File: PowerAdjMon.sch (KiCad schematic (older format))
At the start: 11 parts

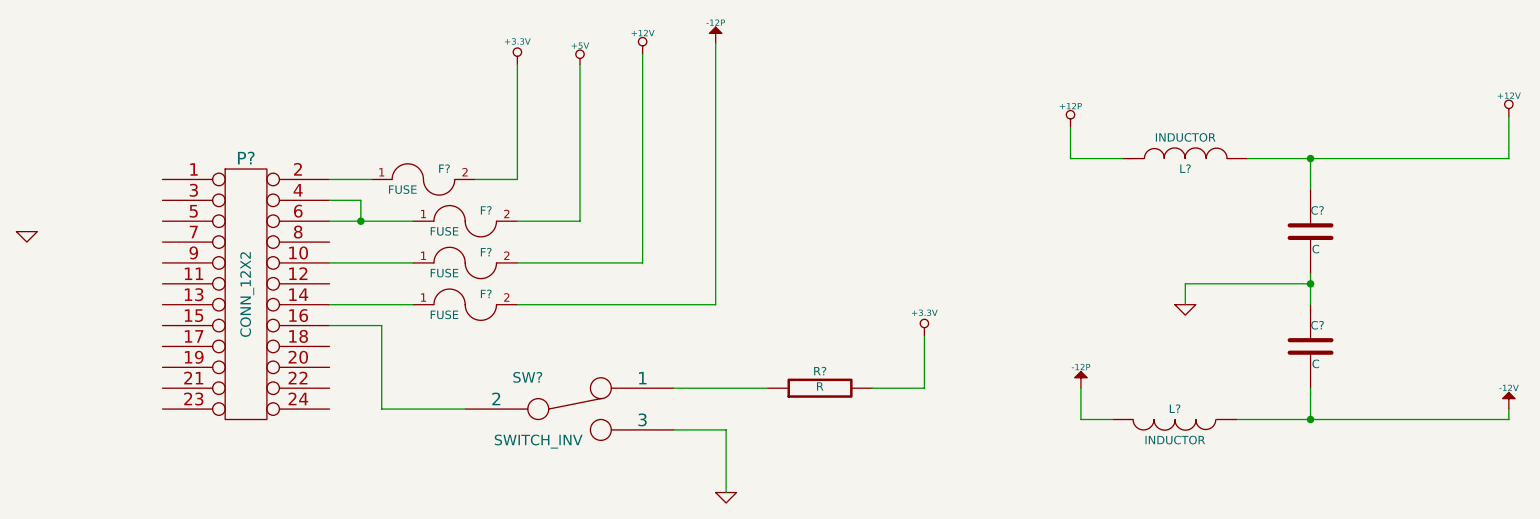
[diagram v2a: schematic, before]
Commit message: Fan/Current mode redo
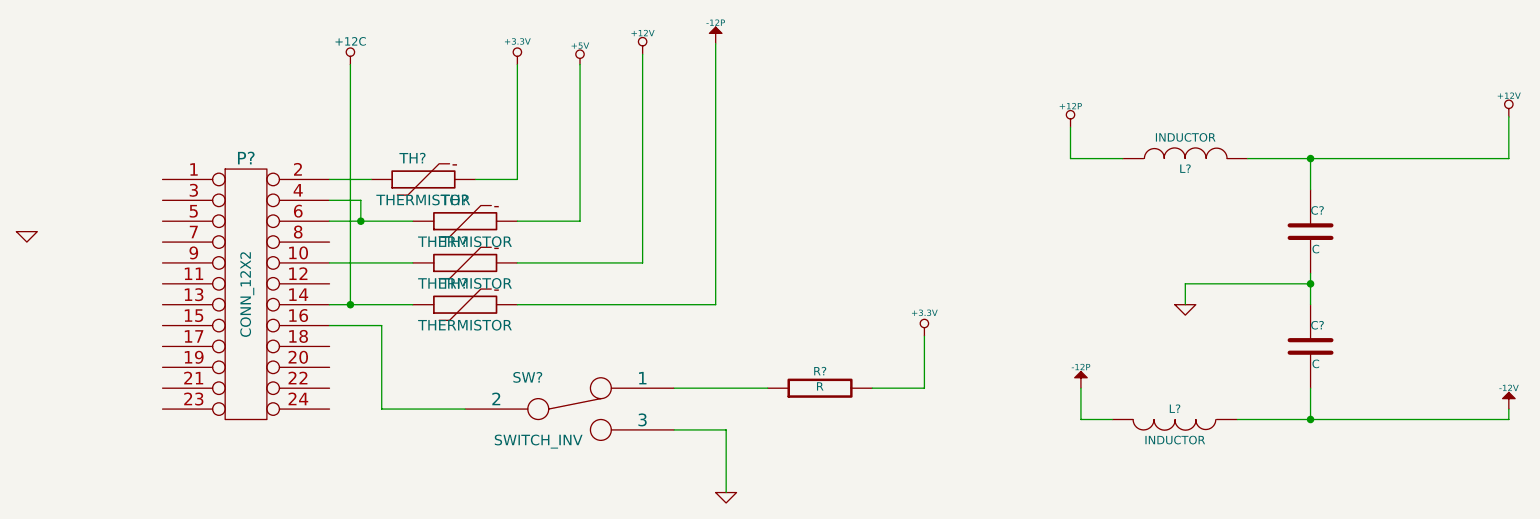
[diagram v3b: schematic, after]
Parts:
- removed F? (x4): FUSE, ~, symbol FUSE
- added TH? (x4): THERMISTOR, symbol THERMISTOR
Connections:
- net +12V: now also TH?.2
- net +3.3V: now also TH?.2
- net +5V: now also TH?.2
- net -12P: now also TH?.2
- net at P?.10 (P10): now also TH?.1
- net +12C: now reaches P?.14 (P14)
- net +12C: now also TH?.1
- net at P?.2 (P2): now also TH?.1
- net at P?.4 (P4), P?.6 (P6): now also TH?.1
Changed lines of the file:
@@
-EESchema Schematic File Version 2  date Sat 08 Feb 2014 11:37:49 PM EST
+EESchema Schematic File Version 2  date Sun 09 Feb 2014 12:22:09 AM EST
 LIBS:power
 LIBS:device
@@
 $EndDescr
 $Comp
+L THERMISTOR TH?
+U 1 1 52F70C96
+P 3150 2250
+F 0 "TH?" V 3250 2300 50  0000 C CNN
+F 1 "THERMISTOR" V 3050 2250 50  0000 C CNN
+	1    3150 2250
+	0    -1   -1   0
+$EndComp
+$Comp
+L THERMISTOR TH?
+U 1 1 52F70C94
+P 3150 2050
+F 0 "TH?" V 3250 2100 50  0000 C CNN
+F 1 "THERMISTOR" V 3050 2050 50  0000 C CNN
+	1    3150 2050
+	0    -1   -1   0
+$EndComp
+$Comp
+L THERMISTOR TH?
+U 1 1 52F70C92
+P 3150 1850
+F 0 "TH?" V 3250 1900 50  0000 C CNN
+F 1 "THERMISTOR" V 3050 1850 50  0000 C CNN
+	1    3150 1850
+	0    -1   -1   0
+$EndComp
+$Comp
+L THERMISTOR TH?
+U 1 1 52F70C8B
+P 2950 1650
+F 0 "TH?" V 3050 1700 50  0000 C CNN
+F 1 "THERMISTOR" V 2850 1650 50  0000 C CNN
+	1    2950 1650
+	0    -1   -1   0
+$EndComp
+$Comp
+L +12C #PWR?
+U 1 1 52F70C06
+P 2600 1100
+F 0 "#PWR?" H 2600 1070 30  0001 C CNN
+F 1 "+12C" H 2600 1210 40  0000 C CNN
+	1    2600 1100
+	1    0    0    -1
+$EndComp
+Connection ~ 2600 2250
+Wire Wire Line
+	2600 2250 2600 1100
+Connection ~ 7200 2800
+Wire Wire Line
+	8150 2750 8150 2800
+Connection ~ 7200 1550
+Wire Wire Line
+	8150 1350 8150 1550
+Wire Wire Line
+	8150 1550 6900 1550
+Wire Wire Line
+	7200 1700 7200 1550
+Wire Wire Line
+	7200 2800 7200 2650
+Wire Wire Line
+	8150 2800 6850 2800
+Connection ~ 7200 2150
+Wire Wire Line
+	7200 2150 6600 2150
+Wire Wire Line
+	6600 2150 6600 2250
+Wire Wire Line
+	7200 2100 7200 2250
+Wire Wire Line
+	6300 1550 6050 1550
+Wire Wire Line
+	6050 1550 6050 1400
+Wire Wire Line
+	6250 2800 6100 2800
+Wire Wire Line
+	6100 2800 6100 2650
+Wire Wire Line
+	5350 2400 5350 2650
+Wire Wire Line
+	5350 2650 5100 2650
+Wire Wire Line
+	4150 2650 4600 2650
+Wire Wire Line
+	4400 3150 4400 2850
+Wire Wire Line
+	4400 2850 4150 2850
+Wire Wire Line
+	3150 2750 2750 2750
+Wire Wire Line
+	2750 2750 2750 2350
+Wire Wire Line
+	2750 2350 2500 2350
+Wire Wire Line
+	4350 1000 4350 2250
+Wire Wire Line
+	4350 2250 3400 2250
+Wire Wire Line
+	4000 1050 4000 2050
+Wire Wire Line
+	4000 2050 3400 2050
+Wire Wire Line
+	2500 2250 2900 2250
+Wire Wire Line
+	2500 2050 2900 2050
+Wire Wire Line
+	3700 1100 3700 1850
+Wire Wire Line
+	3700 1850 3400 1850
+Connection ~ 2650 1850
+Wire Wire Line
+	2650 1850 2650 1750
+Wire Wire Line
+	2650 1750 2500 1750
+Wire Wire Line
+	2500 1850 2900 1850
+Wire Wire Line
+	3400 1100 3400 1650
+Wire Wire Line
+	3400 1650 3200 1650
+Wire Wire Line
+	2500 1650 2700 1650
+$Comp
 L CONN_12X2 P?
 U 1 1 52F45305
@@
 F 1 "+5V" H 3700 1190 30  0000 C CNN
 	1    3700 1100
-	1    0    0    -1
-$EndComp
-$Comp
-L FUSE F?
-U 1 1 52F4550E
-P 2950 1650
-F 0 "F?" H 3050 1700 40  0000 C CNN
-F 1 "FUSE" H 2850 1600 40  0000 C CNN
-F 2 "~" H 2950 1650 60  0000 C CNN
-F 3 "~" H 2950 1650 60  0000 C CNN
-	1    2950 1650
-	1    0    0    -1
-$EndComp
-$Comp
-L FUSE F?
-U 1 1 52F4551B
-P 3150 1850
-F 0 "F?" H 3250 1900 40  0000 C CNN
-F 1 "FUSE" H 3050 1800 40  0000 C CNN
-F 2 "~" H 3150 1850 60  0000 C CNN
-F 3 "~" H 3150 1850 60  0000 C CNN
-	1    3150 1850
-	1    0    0    -1
-$EndComp
-$Comp
-L FUSE F?
-U 1 1 52F45521
-P 3150 2050
-F 0 "F?" H 3250 2100 40  0000 C CNN
-F 1 "FUSE" H 3050 2000 40  0000 C CNN
-F 2 "~" H 3150 2050 60  0000 C CNN
-F 3 "~" H 3150 2050 60  0000 C CNN
-	1    3150 2050
-	1    0    0    -1
-$EndComp
-$Comp
-L FUSE F?
-U 1 1 52F45527
-P 3150 2250
-F 0 "F?" H 3250 2300 40  0000 C CNN
-F 1 "FUSE" H 3050 2200 40  0000 C CNN
-F 2 "~" H 3150 2250 60  0000 C CNN
-F 3 "~" H 3150 2250 60  0000 C CNN
-	1    3150 2250
 	1    0    0    -1
 $EndComp
@@
 	1    0    0    -1
 $EndComp
-Wire Wire Line
-	2500 1650 2700 1650
-Wire Wire Line
-	3200 1650 3400 1650
-Wire Wire Line
-	3400 1650 3400 1100
-Wire Wire Line
-	2500 1850 2900 1850
-Wire Wire Line
-	2500 1750 2650 1750
-Wire Wire Line
-	2650 1750 2650 1850
-Connection ~ 2650 1850
-Wire Wire Line
-	3400 1850 3700 1850
-Wire Wire Line
-	3700 1850 3700 1100
-Wire Wire Line
-	2500 2050 2900 2050
-Wire Wire Line
-	2500 2250 2900 2250
 $Comp
 L +12V #PWR?
@@
 	1    0    0    -1
 $EndComp
-Wire Wire Line
-	3400 2050 4000 2050
-Wire Wire Line
-	4000 2050 4000 1050
 $Comp
 L -12P #PWR?
@@
 	1    0    0    -1
 $EndComp
-Wire Wire Line
-	3400 2250 4350 2250
-Wire Wire Line
-	4350 2250 4350 1000
 $Comp
 L R R?
@@
 	0    -1   -1   0
 $EndComp
-Wire Wire Line
-	2500 2350 2750 2350
-Wire Wire Line
-	2750 2350 2750 2750
-Wire Wire Line
-	2750 2750 3150 2750
 $Comp
 L GND #PWR?
@@
 	1    0    0    -1
 $EndComp
-Wire Wire Line
-	4150 2850 4400 2850
-Wire Wire Line
-	4400 2850 4400 3150
-Wire Wire Line
-	4150 2650 4600 2650
 $Comp
 L +3.3V #PWR?
@@
 	1    0    0    -1
 $EndComp
-Wire Wire Line
-	5100 2650 5350 2650
-Wire Wire Line
-	5350 2650 5350 2400
 $Comp
 L INDUCTOR L?
@@
 	1    0    0    -1
 $EndComp
-Wire Wire Line
-	6100 2650 6100 2800
-Wire Wire Line
-	6100 2800 6250 2800
-Wire Wire Line
-	6050 1400 6050 1550
-Wire Wire Line
-	6050 1550 6300 1550
-Wire Wire Line
-	7200 2100 7200 2250
-Wire Wire Line
-	6600 2150 6600 2250
-Wire Wire Line
-	6600 2150 7200 2150
-Connection ~ 7200 2150
-Wire Wire Line
-	6850 2800 8150 2800
-Wire Wire Line
-	7200 2800 7200 2650
-Wire Wire Line
-	7200 1700 7200 1550
-Wire Wire Line
-	6900 1550 8150 1550
 $Comp
 L +12V #PWR?
@@
 	1    0    0    -1
 $EndComp
-Wire Wire Line
-	8150 1550 8150 1350
-Connection ~ 7200 1550
-Wire Wire Line
-	8150 2800 8150 2750
-Connection ~ 7200 2800
 $EndSCHEMATC
